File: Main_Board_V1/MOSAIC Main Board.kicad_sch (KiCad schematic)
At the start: 82 parts, among them J1 CONN E, J10 QWIIC_RIGHT_ANGLE, J11 Vertical Qwiic Connector, J12 CONN E, J13 CONN E, J14 35RAPC4BH3 CONN 3.5MM, J2 CONN E, J3 CONN E, J4 CONN HEADER VERT 10POS 1.27MM, J5 USB TYPE C R/A SMT 16PIN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

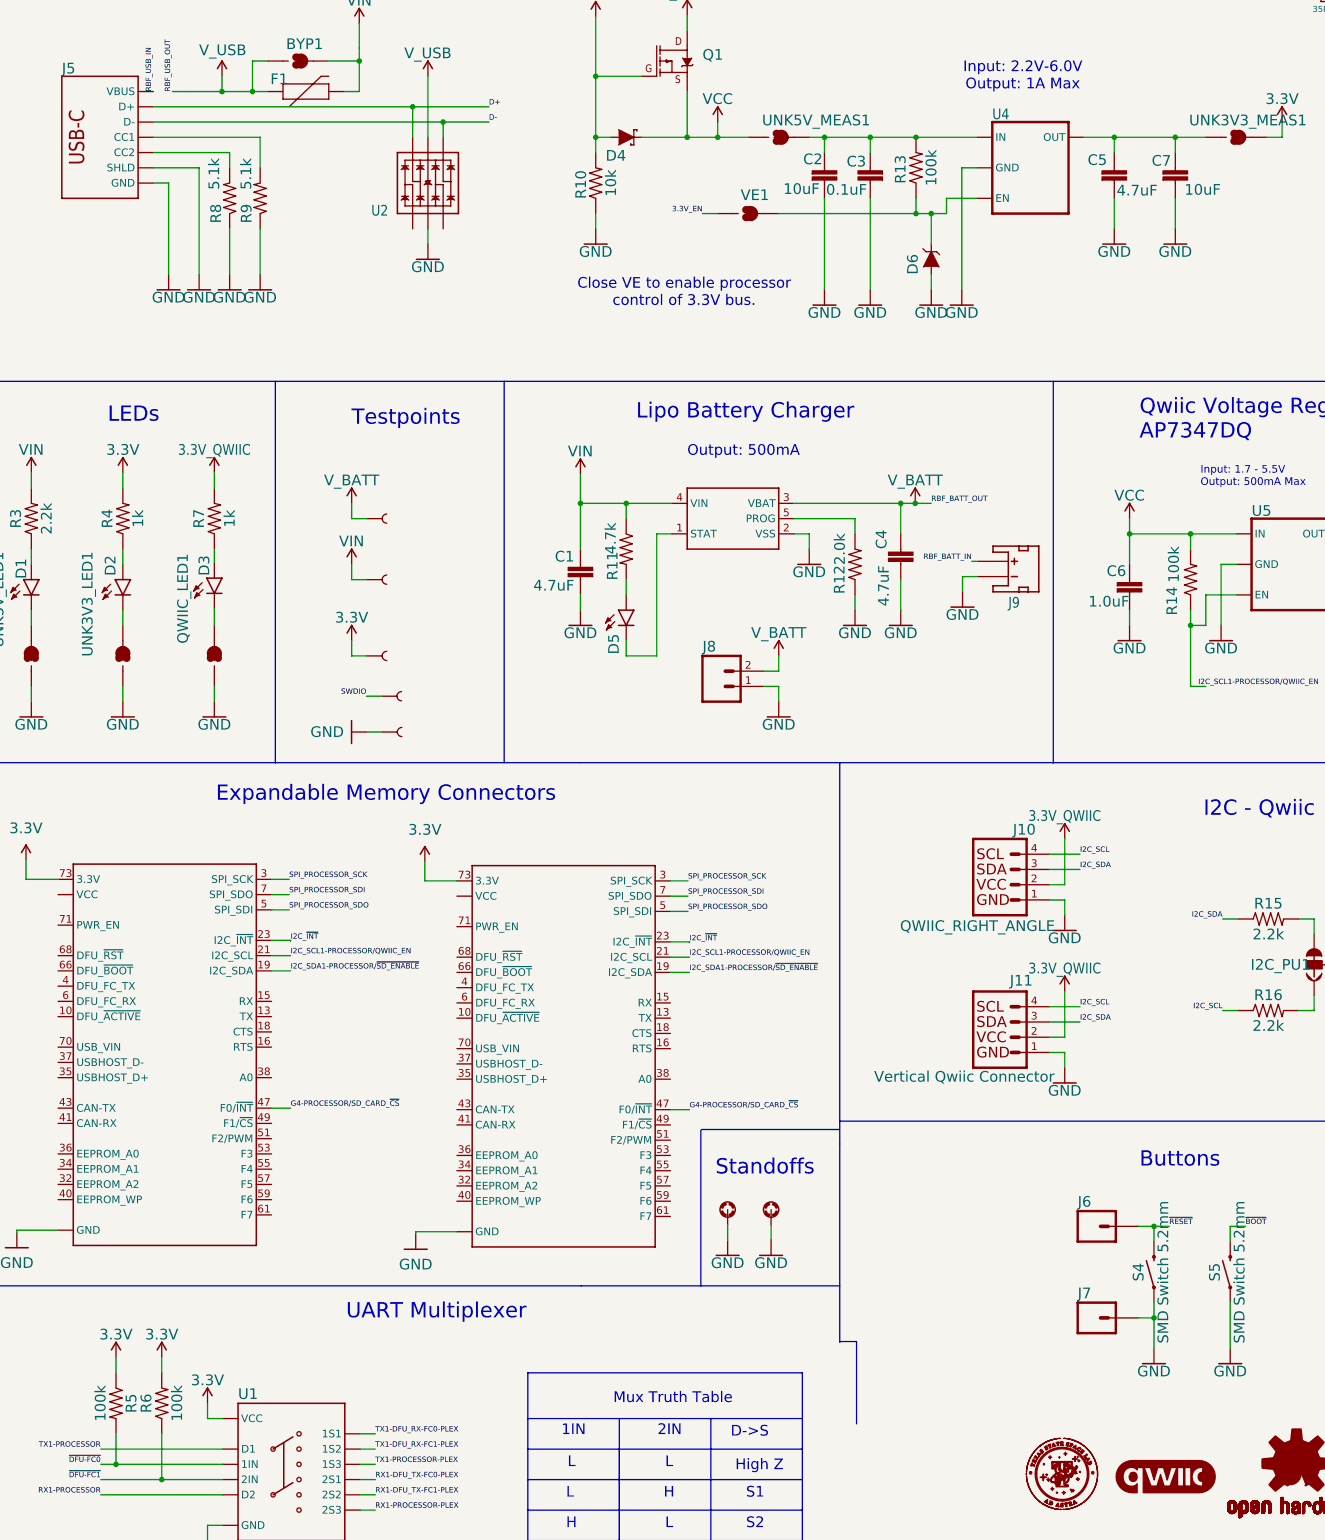
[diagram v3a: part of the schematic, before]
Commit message: updating JLCPCB comp sources
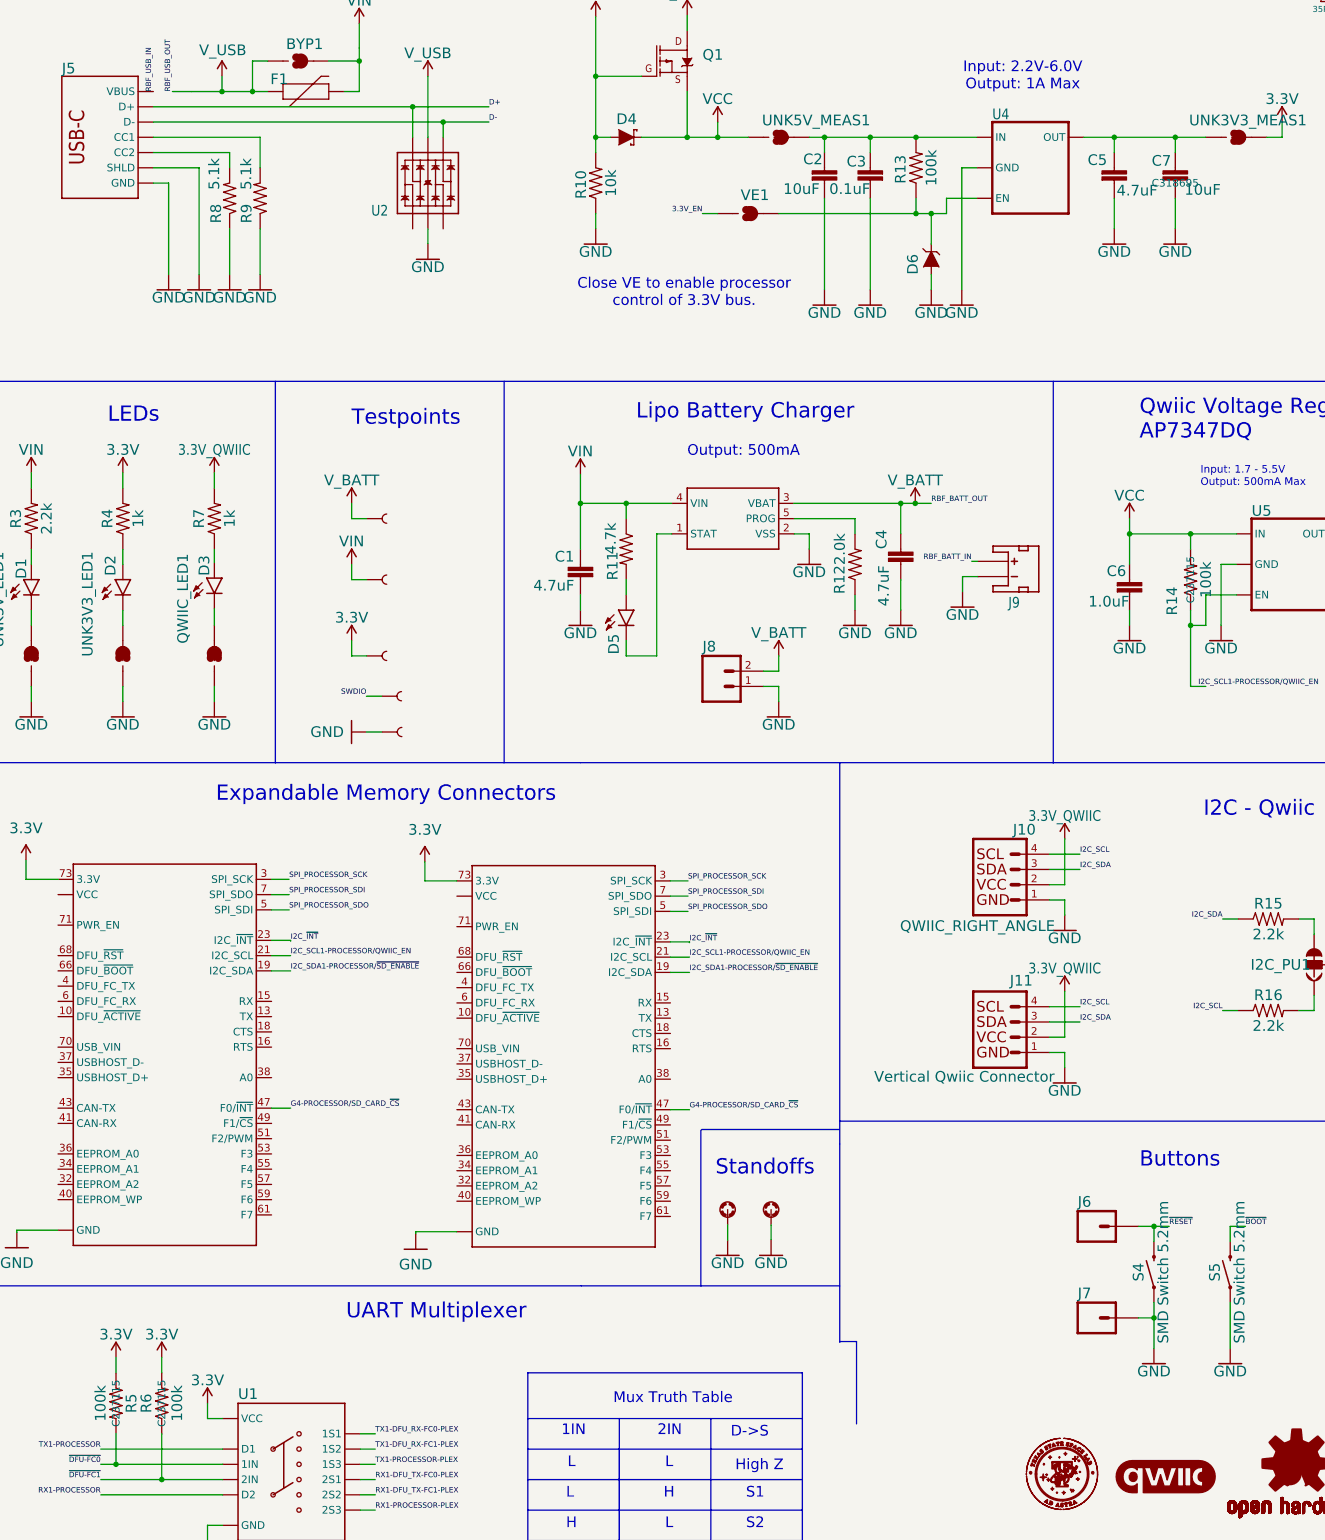
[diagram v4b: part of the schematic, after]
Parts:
- C2: JLCPCB Part # (none) -> C318695; Source https://www.digikey.com/en/products/detail/samsung-electro-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 -> (none)
- C3: footprint main_board_footprints_V1.0:0603 -> SparkFun_Main_Board_Double_v22:0603; JLCPCB Part # (none) -> C18212337; Source https://www.mouser.com/ProductDetail/KYOCERA-AVX/KAM21BR71H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 -> (none)
- C7: footprint main_board_footprints_V1.0:0603 -> main_board_footprints_V1.0:0805; JLCPCB Part # (none) -> C318695; Source https://www.digikey.com/en/products/detail/taiyo-yuden/JMK1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 -> (none)
- D4: JLCPCB Part # (none) -> C85098; Source https://www.digikey.com/en/products/detail/diodes-incorpora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 -> (none)
- R13, R14, R5, R6: JLCPCB Part # (none) -> C237115; Source https://www.digikey.com/en/products/detail/stackpole-electr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 -> (none)
- UNK5V_MEAS1, VE1: now left out of the parts list
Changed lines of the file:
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@@
 		(unit 1)
 		(exclude_from_sim no)
-		(in_bom yes)
+		(in_bom no)
 		(on_board yes)
 		(dnp no)
@@
 			)
 		)
-		(property "Footprint" "main_board_footprints_V1.0:0603"
+		(property "Footprint" "main_board_footprints_V1.0:0805"
 			(at 403.098 69.088 0)
 			(effects
@@
 			)
 		)
-		(property "Datasheet" "https://www.yuden.co.jp/productdata/catalog/mlcc06_e.pdf"
+		(property "Datasheet" "https://jlcpcb.com/api/file/downloadByFileSystemAccessId/8588949188905717760"
 			(at 403.098 69.088 0)
 			(effects
@@
 			)
 		)
-		(property "Description" ""
+		(property "Description" "https://jlcpcb.com/partdetail/299824-CL21A106KOCLRNC/C318695"
 			(at 403.098 69.088 0)
 			(effects
@@
 					(size 1.27 1.27)
 				)
+				(hide yes)
 			)
 		)
-		(property "Source" "https://www.digikey.com/en/products/detail/taiyo-yuden/JMK107ABJ106MA-T/4970720"
+		(property "JLCPCB Part #" "C318695"
 			(at 403.098 69.088 0)
 			(effects
@@
 					(size 1.27 1.27)
 				)
-				(hide yes)
 			)
 		)
@@
 			)
 		)
-		(property "Datasheet" "https://mm.digikey.com/Volume0/opasdata/d220001/medias/docus/609/CL21A106KOQNNNE_Spec.pdf"
+		(property "Datasheet" "https://jlcpcb.com/api/file/downloadByFileSystemAccessId/8588949188905717760"
 			(at 344.678 69.088 0)
 			(effects
@@
 			)
 		)
-		(property "Description" ""
+		(property "Description" "https://jlcpcb.com/partdetail/299824-CL21A106KOCLRNC/C318695"
 			(at 344.678 69.088 0)
 			(effects
@@
 					(size 1.27 1.27)
 				)
+				(hide yes)
 			)
 		)
-		(property "Source" "https://www.digikey.com/en/products/detail/samsung-electro-mechanics/CL21A106KOCLRNC/3888057"
+		(property "JLCPCB Part #" "C318695"
 			(at 344.678 69.088 0)
 			(effects
@@
 		)
 		(property "Value" "0.1uF"
-			(at 344.932 71.247 0)
+			(at 352.298 71.12 0)
 			(effects
 				(font
 					(size 1.778 1.778)
 				)
-				(justify right bottom)
+				(justify left bottom)
 			)
 		)
-		(property "Footprint" "main_board_footprints_V1.0:0603"
+		(property "Footprint" "SparkFun_Main_Board_Double_v22:0603"
 			(at 352.298 69.088 0)
 			(effects
@@
 			)
 		)
-		(property "Description" ""
+		(property "Description" "https://jlcpcb.com/partdetail/-KAF21BR71H104JT/C18212337"
 			(at 352.298 69.088 0)
 			(effects
@@
 					(size 1.27 1.27)
 				)
+				(hide yes)
 			)
 		)
-		(property "Source" "https://www.mouser.com/ProductDetail/KYOCERA-AVX/KAM21BR71H104JT?qs=Jm2GQyTW%2Fbic6Zk4McEt6w%3D%3D"
+		(property "JLCPCB Part #" "C18212337"
 			(at 352.298 69.088 0)
 			(effects
@@
 		)
 		(property "Value" "100k"
-			(at 401.828 132.588 0)
+			(at 407.162 135.128 0)
 			(effects
 				(font
@@
 			)
 		)
-		(property "Datasheet" "https://www.seielect.com/catalog/sei-rmcf_rmcp.pdf"
+		(property "Datasheet" "https://jlcpcb.com/api/file/downloadByFileSystemAccessId/8588906178609369088"
 			(at 405.638 135.128 0)
 			(effects
@@
 			)
 		)
-		(property "Description" ""
+		(property "Description" "https://jlcpcb.com/partdetail/sei_stackpole_elec-RMCF0603JT100K/C237115"
 			(at 405.638 135.128 0)
 			(effects
@@
 					(size 1.27 1.27)
 				)
+				(hide yes)
 			)
 		)
-		(property "Source" "https://www.digikey.com/en/products/detail/stackpole-electronics-inc/RMCF0603FT100K/1761112"
+		(property "JLCPCB Part #" "C237115"
 			(at 405.638 135.128 0)
 			(effects
@@
 					(size 1.27 1.27)
 				)
-				(hide yes)
 			)
 		)
@@
 		(unit 1)
 		(exclude_from_sim no)
-		(in_bom yes)
+		(in_bom no)
 		(on_board yes)
 		(dnp no)
@@
 			)
 		)
-		(property "Datasheet" "https://www.seielect.com/catalog/sei-rmcf_rmcp.pdf"
+		(property "Datasheet" "https://jlcpcb.com/api/file/downloadByFileSystemAccessId/8588906178609369088"
 			(at 359.918 66.548 0)
 			(effects
@@
 			)
 		)
-		(property "Description" ""
+		(property "Description" "https://jlcpcb.com/partdetail/sei_stackpole_elec-RMCF0603JT100K/C237115"
 			(at 359.918 66.548 0)
 			(effects
@@
 					(size 1.27 1.27)
 				)
+				(hide yes)
 			)
 		)
-		(property "Source" "https://www.digikey.com/en/products/detail/stackpole-electronics-inc/RMCF0603JT100K/1758100"
+		(property "JLCPCB Part #" "C237115"
 			(at 359.918 66.548 0)
 			(effects
@@
 		(dnp no)
 		(property "Reference" "D4"
-			(at 311.658 63.5 0)
+			(at 313.436 57.404 0)
 			(effects
 				(font
@@
 		)
 		(property "Value" "DIODE SCHOTTKY 40V 3A SMA"
-			(at 309.372 66.294 0)
+			(at 309.118 63.5 0)
 			(effects
 				(font
@@
 			)
 		)
-		(property "Datasheet" "https://www.diodes.com/assets/Datasheets/ds30891.pdf"
+		(property "Datasheet" "https://jlcpcb.com/api/file/downloadByFileSystemAccessId/8588880424093290496"
 			(at 311.658 61.468 0)
 			(effects
@@
 			)
 		)
-		(property "Description" ""
+		(property "Description" "https://jlcpcb.com/partdetail/DiodesIncorporated-B340A_13F/C85098"
 			(at 311.658 61.468 0)
 			(effects
@@
 					(size 1.27 1.27)
 				)
+				(hide yes)
 			)
 		)
-		(property "Source" "https://www.digikey.com/en/products/detail/diodes-incorporated/B340A-13-F/725054?utm_adgroup=&utm_term=&utm_content=&gad_source=1"
-			(at 311.658 61.468 0)
+		(property "JLCPCB Part #" "C85098"
+			(at 312.166 58.42 0)
 			(effects
 				(font
@@
 			)
 		)
-		(property "Datasheet" "https://www.seielect.com/catalog/sei-rmcf_rmcp.pdf"
+		(property "Datasheet" "https://jlcpcb.com/api/file/downloadByFileSystemAccessId/8588906178609369088"
 			(at 234.315 272.288 0)
 			(effects
@@
 			)
 		)
-		(property "Description" ""
+		(property "Description" "https://jlcpcb.com/partdetail/sei_stackpole_elec-RMCF0603JT100K/C237115"
 			(at 234.315 272.288 0)
 			(effects
@@
 					(size 1.27 1.27)
 				)
+				(hide yes)
 			)
 		)
-		(property "Source" "https://www.digikey.com/en/products/detail/stackpole-electronics-inc/RMCF0603FT100K/1761112"
+		(property "JLCPCB Part #" "C237115"
 			(at 234.315 272.288 0)
 			(effects
@@
 					(size 1.27 1.27)
 				)
-				(hide yes)
 			)
 		)
@@
 			)
 		)
-		(property "Datasheet" "https://www.seielect.com/catalog/sei-rmcf_rmcp.pdf"
+		(property "Datasheet" "https://jlcpcb.com/api/file/downloadByFileSystemAccessId/8588906178609369088"
 			(at 226.695 272.288 0)
 			(effects
@@
 			)
 		)
-		(property "Description" ""
+		(property "Description" "https://jlcpcb.com/partdetail/sei_stackpole_elec-RMCF0603JT100K/C237115"
 			(at 226.695 272.288 0)
 			(effects
@@
 					(size 1.27 1.27)
 				)
+				(hide yes)
 			)
 		)
-		(property "Source" "https://www.digikey.com/en/products/detail/stackpole-electronics-inc/RMCF0603FT100K/1761112"
+		(property "JLCPCB Part #" "C237115"
 			(at 226.695 272.288 0)
 			(effects
@@
 					(size 1.27 1.27)
 				)
-				(hide yes)
 			)
 		)
